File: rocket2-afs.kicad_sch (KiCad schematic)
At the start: 67 parts, among them J1 ARMING_PLUG, J2 POWER, J3 E-MATCH_DROGUE, J4 SWD, J5 E-MATCH_RECOVERY, Q1 Q_NMOS_GSD, Q2 Q_NMOS_GSD, Q3 Q_NMOS_GSD, Q4 Q_NMOS_GSD, Q5 Q_NMOS_GSD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

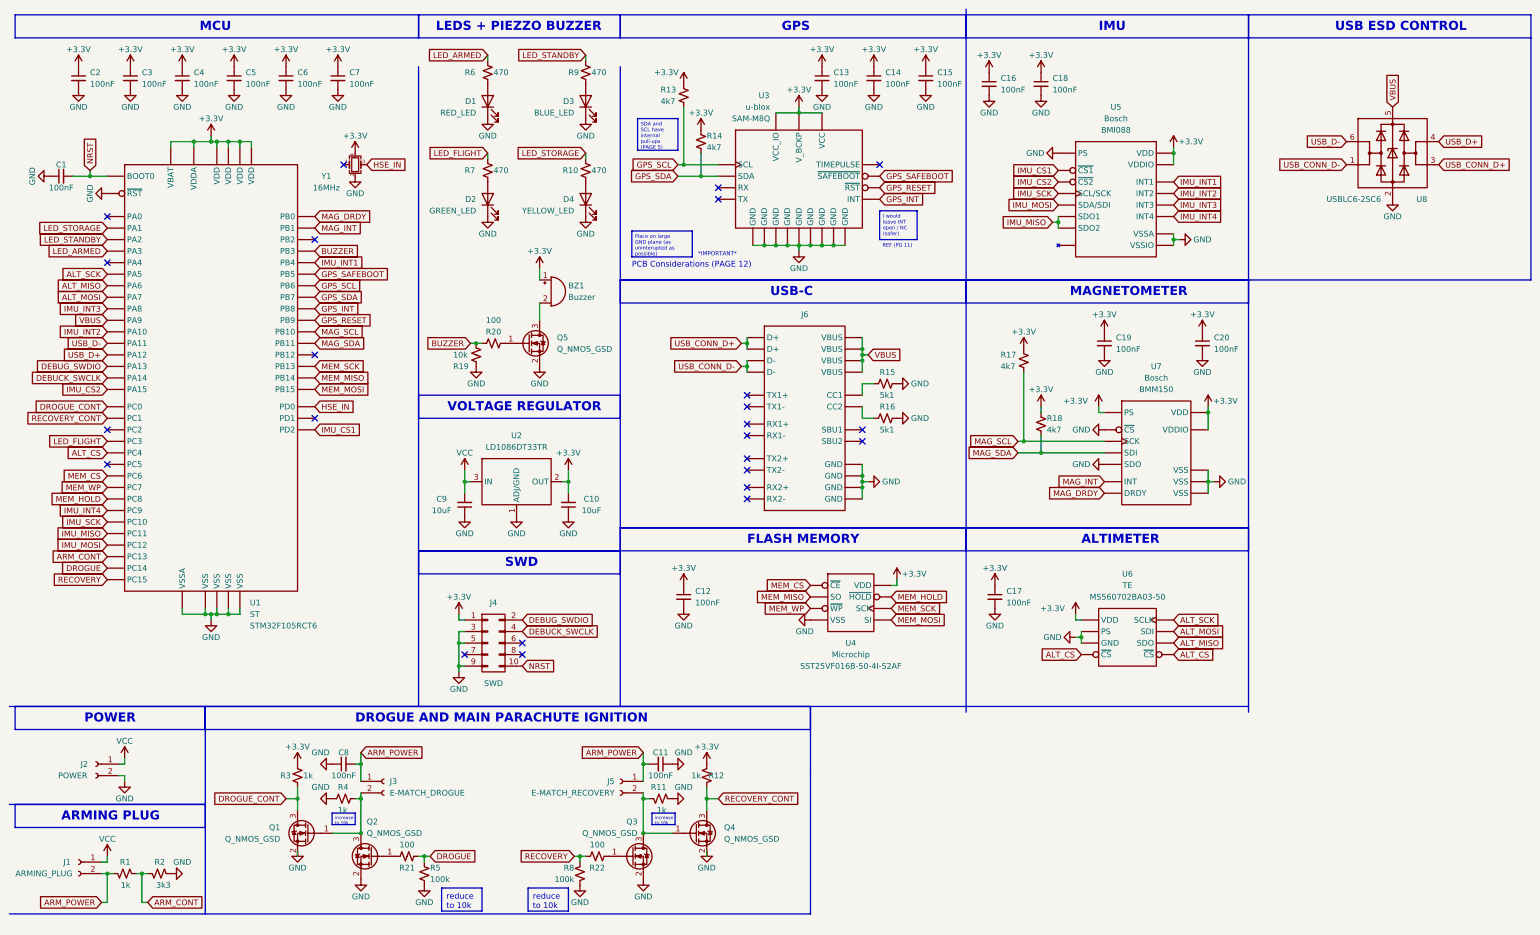
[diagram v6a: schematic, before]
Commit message: Completely Remade PCB to adjust for GPS GND Shield
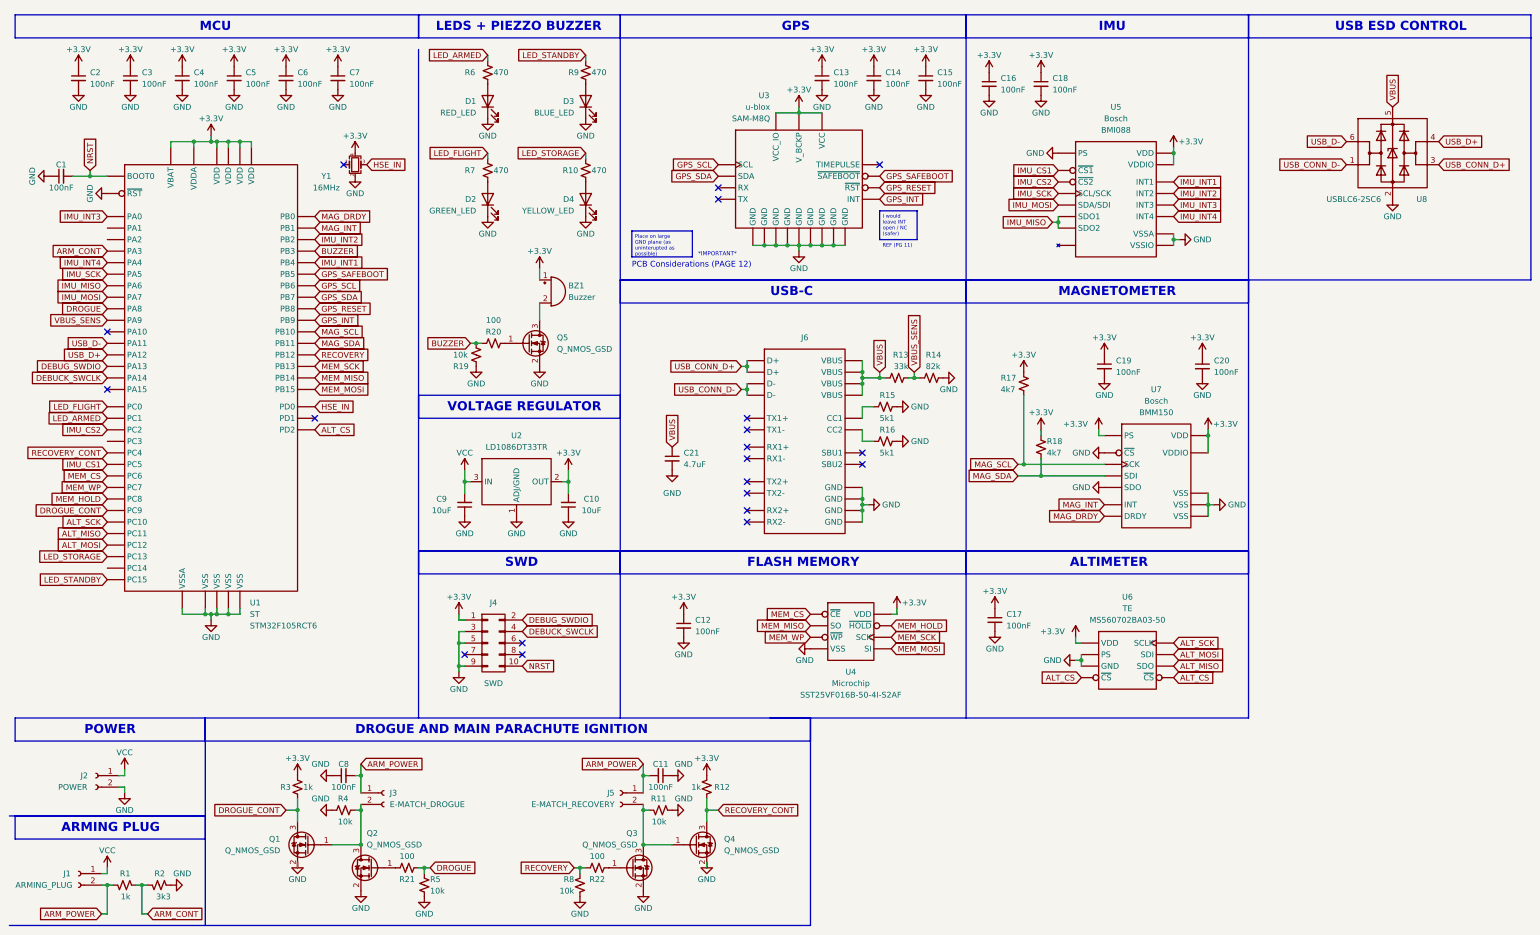
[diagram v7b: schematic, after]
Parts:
- added C21: 4.7uF, Capacitor_SMD:C_0603_1608Metric, symbol Device:C_Small
- BZ1: Manufacturer (none) -> CUI Devices; Part # (none) -> CMI-9653S-SMT-TR
- C1, C10, C11, C12, C13, C14, C15, C16, C17, C18, C19, C2, C20, C3, C4, C5, C6, C7, C8, C9: Manufacturer (none) -> Generic; Part # (none) -> Generic 0603 6.3V 100nF Power Decoupling Cap
- D1: Manufacturer (none) -> Generic; Part # (none) -> Generic Red LED
- D2: Manufacturer (none) -> Generic; Part # (none) -> Generic Green LED
- D3: Manufacturer (none) -> Generic; Part # (none) -> Generic Blue LED
- D4: Manufacturer (none) -> Generic; Part # (none) -> Generic Yellow LED
- J1, J2, J3, J5: Manufacturer (none) -> Generic; Part # (none) -> Generic Horizontal TH P5.08mm Screw Fastened
- J4: Manufacturer (none) -> Generic; Part # (none) -> Generic 2x05 P1.27mm Vertical SMD
- J6: Manufacturer (none) -> GCT; Part # (none) -> USB4105-GF-A
- Q1, Q2, Q3, Q4, Q5: Manufacturer (none) -> nexperia; Part # (none) -> PMV30UN2
- R1, R12, R3: Manufacturer (none) -> Generic; Part # (none) -> Generic 0603 1k 5% Res
- R10, R6, R7, R9: Manufacturer (none) -> Generic; Part # (none) -> Generic 0603 470 5% Res
- R11, R4: value 1k -> 10k; Manufacturer (none) -> Generic; Part # (none) -> Generic 0603 10k 5% Res
- R13: value 4k7 -> 33k; Manufacturer (none) -> Generic; Part # (none) -> Generic 0603 33k 5% Res
- R14: value 4k7 -> 82k; Manufacturer (none) -> Generic; Part # (none) -> Generic 0603 82k 5% Res
- R15, R16: Manufacturer (none) -> Generic; Part # (none) -> Generic 0603 5.1k 1% Res
- R17, R18: Manufacturer (none) -> Generic; Part # (none) -> Generic 0603 4.7k 5% Res
- R19: Manufacturer (none) -> Generic; Part # (none) -> Generic 0603 10k 5% Res
- R2: Manufacturer (none) -> Generic; Part # (none) -> Generic 0603 3.3k 5% Res
- R20, R21, R22: Manufacturer (none) -> Generic; Part # (none) -> Generic 0603 100 5% Res
- R5, R8: value 100k -> 10k; Manufacturer (none) -> Generic; Part # (none) -> Generic 0603 10k 5% Res
- U2: Manufacturer (none) -> ST; Part # (none) -> LD1086DT33TR
- U8: Manufacturer (none) -> ST; Part # (none) -> USBLC6-2SC6
- Y1: Manufacturer (none) -> RoHS; Part # (none) -> ECS-1633
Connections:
- net +3.3V: no longer R13.1, R14.1
- net ALT_CS: now also U1.54 (PD2); no longer U1.24 (PC4)
- net ALT_MISO: now also U1.52 (PC11); no longer U1.22 (PA6)
- net ALT_MOSI: now also U1.53 (PC12); no longer U1.23 (PA7)
- net ALT_SCK: now also U1.51 (PC10); no longer U1.21 (PA5)
- net ARM_CONT: now also U1.17 (PA3); no longer U1.2 (PC13)
- net DROGUE: now also U1.41 (PA8); no longer U1.3 (PC14)
- net DROGUE_CONT: now also U1.40 (PC9); no longer U1.8 (PC0)
- net GND: now also R14.1, C21.2
- net GPS_INT: now also U1.62 (PB9); no longer U1.61 (PB8)
- net GPS_RESET: now also U1.61 (PB8); no longer U1.62 (PB9)
- net GPS_SCL: no longer R13.2
- net GPS_SDA: no longer R14.2
- net IMU_CS1: now also U1.25 (PC5); no longer U1.54 (PD2)
- net IMU_CS2: now also U1.10 (PC2); no longer U1.50 (PA15)
- net IMU_INT2: now also U1.28 (PB2); no longer U1.43 (PA10)
- net IMU_INT3: now also U1.14 (PA0); no longer U1.41 (PA8)
- net IMU_INT4: now also U1.20 (PA4); no longer U1.40 (PC9)
- net IMU_MISO: now also U1.22 (PA6); no longer U1.52 (PC11)
- net IMU_MOSI: now also U1.23 (PA7); no longer U1.53 (PC12)
- net IMU_SCK: now also U1.21 (PA5); no longer U1.51 (PC10)
- net LED_ARMED: now also U1.9 (PC1); no longer U1.17 (PA3)
- net LED_FLIGHT: now also U1.8 (PC0); no longer U1.11 (PC3)
- net LED_STANDBY: now also U1.4 (PC15); no longer U1.16 (PA2)
- net LED_STORAGE: now also U1.2 (PC13); no longer U1.15 (PA1)
- net RECOVERY: now also U1.33 (PB12); no longer U1.4 (PC15)
- net RECOVERY_CONT: now also U1.24 (PC4); no longer U1.9 (PC1)
- net VBUS: now also R13.1, C21.1; no longer U1.42 (PA9)
- new net VBUS_SENS: R13.2, R14.2, U1.42 (PA9)
- no-connect marks 24 -> 20
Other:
- moved on the sheet: C11, C12, C17, C19, C20, C8, J1, J2, J3, J5, J6, Q1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

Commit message: Completely Remade PCB to Space out Components
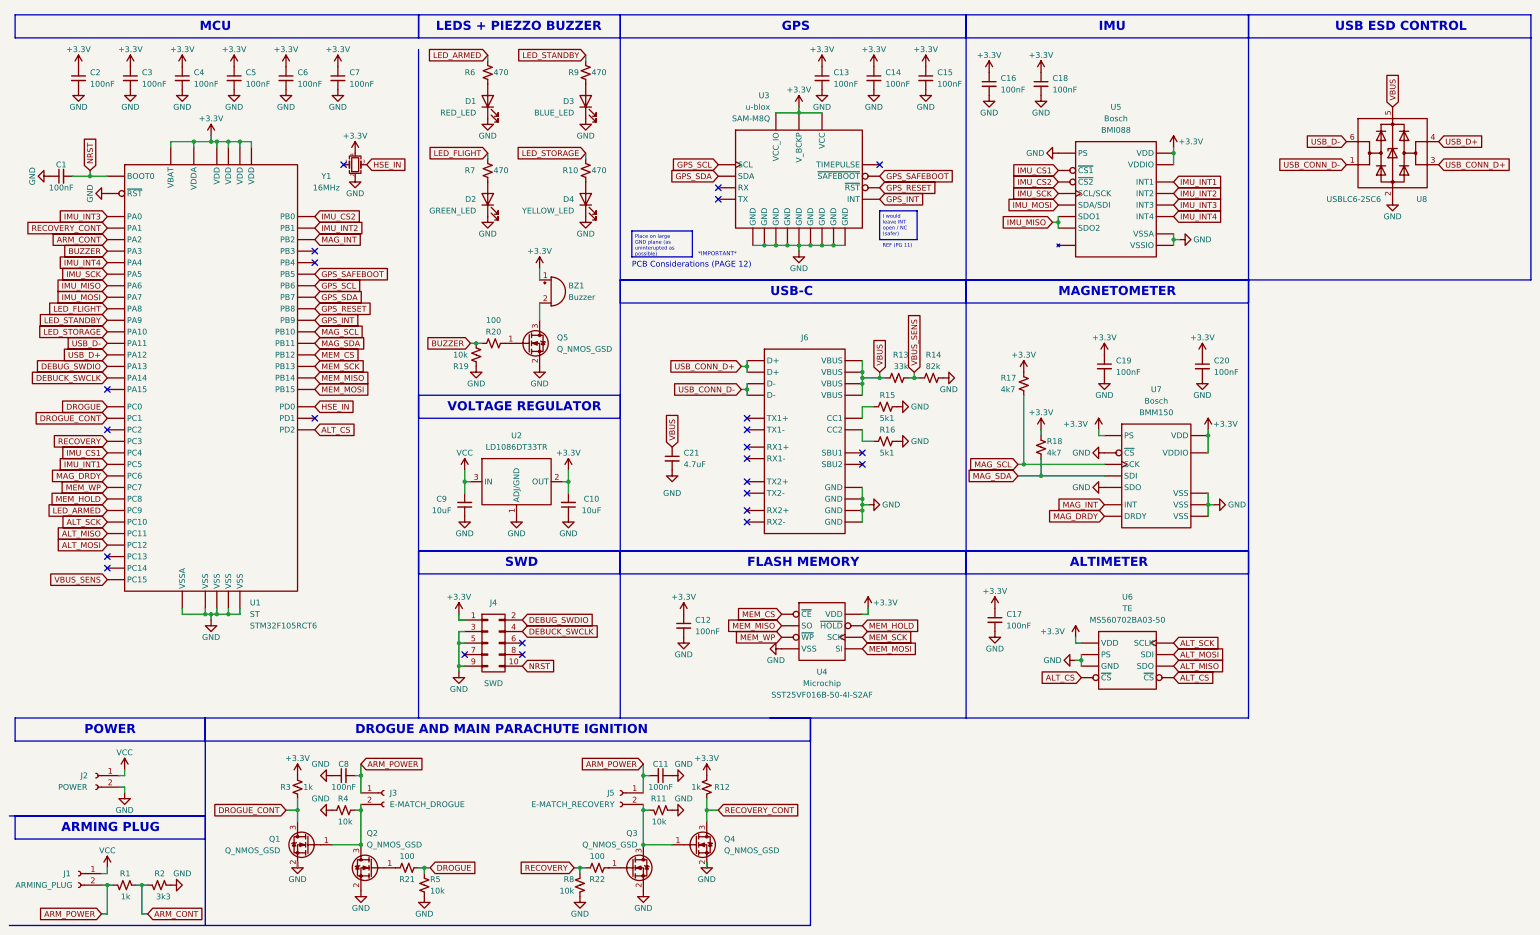
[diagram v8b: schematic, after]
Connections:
- net ARM_CONT: now also U1.16 (PA2); no longer U1.17 (PA3)
- net BUZZER: now also U1.17 (PA3); no longer U1.55 (PB3)
- net DROGUE: now also U1.8 (PC0); no longer U1.41 (PA8)
- net DROGUE_CONT: now also U1.9 (PC1); no longer U1.40 (PC9)
- net IMU_CS1: now also U1.24 (PC4); no longer U1.25 (PC5)
- net IMU_CS2: now also U1.26 (PB0); no longer U1.10 (PC2)
- net IMU_INT1: now also U1.25 (PC5); no longer U1.56 (PB4)
- net IMU_INT2: now also U1.27 (PB1); no longer U1.28 (PB2)
- net LED_ARMED: now also U1.40 (PC9); no longer U1.9 (PC1)
- net LED_FLIGHT: now also U1.41 (PA8); no longer U1.8 (PC0)
- net LED_STANDBY: now also U1.42 (PA9); no longer U1.4 (PC15)
- net LED_STORAGE: now also U1.43 (PA10); no longer U1.2 (PC13)
- net MAG_DRDY: now also U1.37 (PC6); no longer U1.26 (PB0)
- net MAG_INT: now also U1.28 (PB2); no longer U1.27 (PB1)
- net MEM_CS: now also U1.33 (PB12); no longer U1.37 (PC6)
- net RECOVERY: now also U1.11 (PC3); no longer U1.33 (PB12)
- net RECOVERY_CONT: now also U1.15 (PA1); no longer U1.24 (PC4)
- net VBUS_SENS: now also U1.4 (PC15); no longer U1.42 (PA9)
- no-connect marks 20 -> 24
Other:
- moved on the sheet: U4
